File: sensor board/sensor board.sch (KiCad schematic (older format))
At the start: 25 parts, among them IC1 AD5933YRSZ, IC2 MAX86141ENP+, J1 502078-1710

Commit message: sensor board part numbers review
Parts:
- C1, C6: Digikey Part Number (none) -> 311-1729-2-ND; Field4 https://www.mouser.ee/ProductDetail/Yageo/CC0402MRX5R5BB106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 -> (none); Mouser Price/Stock (none) -> https://www.mouser.ee/ProductDetail/Yageo/CC0402MRX5R5BB106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; Price 0.23 -> 0.22
- C2: renamed from C3; Digikey Part Number (none) -> 311-1640-2-ND; Field4 https://www.mouser.ee/ProductDetail/Yageo/CC0402FRNPO9BN100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 -> (none); Mouser Price/Stock (none) -> https://www.mouser.ee/ProductDetail/Yageo/CC0402FRNPO9BN100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
- C3: renamed from C2; Digikey Part Number (none) -> 311-1438-2-ND; Field4 https://www.mouser.ee/ProductDetail/Yageo/CC0402KRX5R5BB105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 -> (none); Mouser Price/Stock (none) -> https://www.mouser.ee/ProductDetail/Yageo/CC0402KRX5R5BB105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
- C4: Digikey Part Number (none) -> 311-3479-2-ND; Field4 https://www.mouser.ee/ProductDetail/Yageo/CC0402MRX5R5BB226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 -> (none); Mouser Price/Stock (none) -> https://www.mouser.ee/ProductDetail/Yageo/CC0402MRX5R5BB226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
- C5: Digikey Part Number (none) -> 311-3340-2-ND; Field4 https://www.mouser.ee/ProductDetail/Yageo/CC0402KRX5R5BB104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 -> (none); Mouser Price/Stock (none) -> https://www.mouser.ee/ProductDetail/Yageo/CC0402KRX5R5BB104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
- D1: Field4 https://www.mouser.ee/ProductDetail/OSRAM-Opto-Semiconducto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 -> (none); Mouser Price/Stock (none) -> https://www.mouser.ee/ProductDetail/OSRAM-Opto-Semiconducto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
- D2, D3: Digikey Part Number (none) -> VEMD8080TR-ND
- IC1: Digikey Part Number (none) -> AD5933YRSZ-ND
- IC2: Digikey Part Number (none) -> MAX86141ENP+-ND
- J1: Digikey Part Number (none) -> WM14446TR-ND
- L1: footprint LQW15DN100M00D -> Horace:LQW15DN150M00D; Digikey Part Number (none) -> 490-18069-2-ND
- R1, R10, R2, R5: Digikey Part Number (none) -> 541-4062-2-ND; Field4 https://www.mouser.ee/ProductDetail/Vishay-Dale/CRCW0402000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 -> (none); Mouser Price/Stock (none) -> https://www.mouser.ee/ProductDetail/Vishay-Dale/CRCW0402000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
- R3, R4: Digikey Part Number (none) -> 541-4276-2-ND; Field4 https://www.mouser.ee/ProductDetail/Vishay-Dale/CRCW010010K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 -> (none); Mouser Price/Stock (none) -> https://www.mouser.ee/ProductDetail/Vishay-Dale/CRCW010010K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
- R6, R8, R9: Digikey Part Number (none) -> 541-4279-2-ND; Field4 https://www.mouser.ee/ProductDetail/Vishay-Dale/CRCW01001K0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 -> (none); Mouser Price/Stock (none) -> https://www.mouser.ee/ProductDetail/Vishay-Dale/CRCW01001K0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; Price 0.15 -> 0.14
- R7: Digikey Part Number (none) -> 541-4279-2-ND; Mouser Price/Stock (none) -> https://www.mouser.ee/ProductDetail/Vishay-Dale/CRCW01001K0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; Price 0.15 -> 0.14
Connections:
- net at IC1.6 (VOUT): now also L1.1
- net at L1.2: now also C2.2, TP1.1
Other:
- moved on the sheet: L1

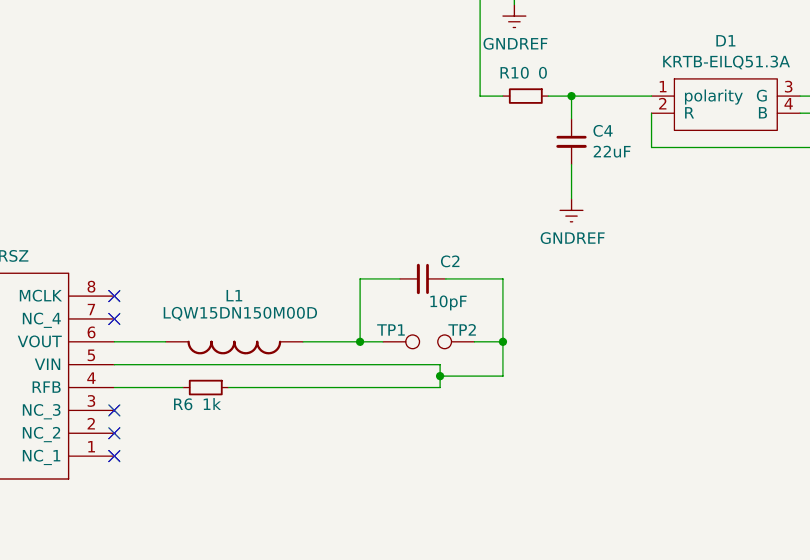
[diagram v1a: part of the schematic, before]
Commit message: added impedance probe pins
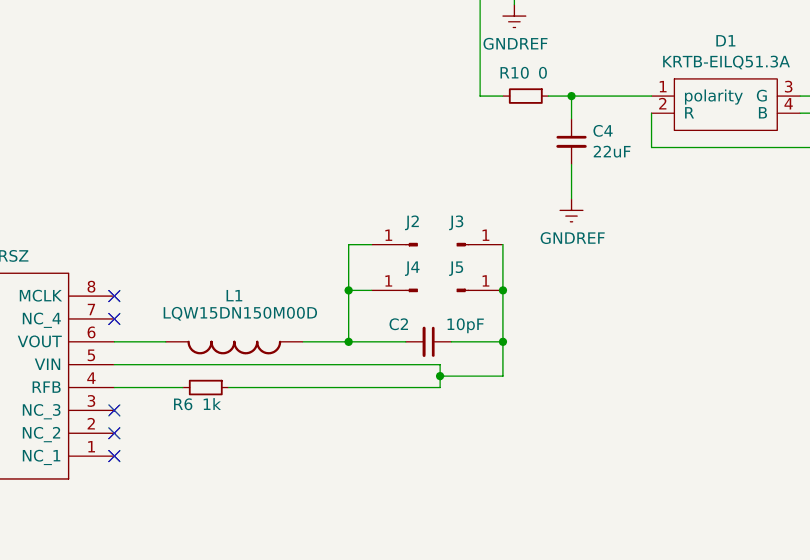
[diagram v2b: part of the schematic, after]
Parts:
- removed TP1, TP2: TestPoint, TestPoint:TestPoint_Pad_D1.5mm, symbol Connector:TestPoint
- added J2, J3, J4, J5: Probe_01_male, Horace:Probe_01_male, symbol Horace:Probe_01_male
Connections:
- net at C2.1, IC1.5 (VIN), R6.1: now also J3.1 (Pin_1), J5.1 (Pin_1)
- net at C2.2, L1.2: now also J2.1 (Pin_1), J4.1 (Pin_1)
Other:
- moved on the sheet: C2
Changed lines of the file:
@@
 L Device:C_Small C2
 U 1 1 6002A88D
-P 4250 5550
-F 0 "C2" V 4175 5625 50  0000 L CNN
-F 1 "10pF" V 4350 5575 50  0000 L CNN
-F 2 "Capacitor_SMD:C_0402_1005Metric" H 4250 5550 50  0001 C CNN
-F 3 "https://www.mouser.ee/datasheet/2/447/yageo_yago_s_a0009251638_1-1991554.pdf" H 4250 5550 50  0001 C CNN
-F 4 "https://www.mouser.ee/ProductDetail/Yageo/CC0402FRNPO9BN100/?qs=5q%252BqlK8CmJS9pmxsdlpWSg%3D%3" V 4250 5550 50  0001 C CNN "Mouser Price/Stock"
-F 5 "311-1640-2-ND" V 4250 5550 50  0001 C CNN "Digikey Part Number"
-F 6 "0.09" V 4250 5550 50  0001 C CNN "Price"
-	1    4250 5550
+P 4275 5825
+F 0 "C2" V 4200 5650 50  0000 L CNN
+F 1 "10pF" V 4200 5900 50  0000 L CNN
+F 2 "Capacitor_SMD:C_0402_1005Metric" H 4275 5825 50  0001 C CNN
+F 3 "https://www.mouser.ee/datasheet/2/447/yageo_yago_s_a0009251638_1-1991554.pdf" H 4275 5825 50  0001 C CNN
+F 4 "https://www.mouser.ee/ProductDetail/Yageo/CC0402FRNPO9BN100/?qs=5q%252BqlK8CmJS9pmxsdlpWSg%3D%3" V 4275 5825 50  0001 C CNN "Mouser Price/Stock"
+F 5 "311-1640-2-ND" V 4275 5825 50  0001 C CNN "Digikey Part Number"
+F 6 "0.09" V 4275 5825 50  0001 C CNN "Price"
+	1    4275 5825
 	0    1    1    0
 $EndComp
@@
 	4325 5975 4325 6025
 Wire Wire Line
-	4150 5550 3975 5550
-Wire Wire Line
-	3975 5550 3975 5825
-Wire Wire Line
-	3975 5825 4075 5825
-Wire Wire Line
-	4600 5550 4600 5825
-Wire Wire Line
 	4325 5975 4600 5975
 Wire Wire Line
-	4350 5550 4600 5550
-Wire Wire Line
-	4475 5825 4600 5825
-Connection ~ 4600 5825
-Wire Wire Line
-	4600 5825 4600 5975
+	4375 5825 4600 5825
 $Comp
 L Horace:MAX86141ENP+ IC2
@@
 	1    1200 1725
 	1    0    0    -1
-$EndComp
-$Comp
-L Connector:TestPoint TP1
-U 1 1 603606C3
-P 4075 5825
-F 0 "TP1" V 4025 5800 50  0000 L CNN
-F 1 "TestPoint" V 4120 6013 50  0001 L CNN
-F 2 "TestPoint:TestPoint_Pad_D1.5mm" H 4275 5825 50  0001 C CNN
-F 3 "~" H 4275 5825 50  0001 C CNN
-	1    4075 5825
-	0    1    1    0
-$EndComp
-$Comp
-L Connector:TestPoint TP2
-U 1 1 603615F7
-P 4475 5825
-F 0 "TP2" V 4525 5875 50  0000 C CNN
-F 1 "TestPoint" V 4520 6013 50  0001 L CNN
-F 2 "TestPoint:TestPoint_Pad_D1.5mm" H 4675 5825 50  0001 C CNN
-F 3 "~" H 4675 5825 50  0001 C CNN
-	1    4475 5825
-	0    -1   -1   0
 $EndComp
 $Comp
@@
 Wire Wire Line
 	2900 5825 3125 5825
-Connection ~ 3975 5825
 Wire Wire Line
 	2900 5925 4325 5925
@@
 Wire Wire Line
 	4500 4750 4600 4750
-Wire Wire Line
-	3725 5825 3975 5825
+$Comp
+L Horace:Probe_01_male J5
+U 1 1 605103DC
+P 4400 5600
+F 0 "J5" H 4400 5700 50  0000 C CNN
+F 1 "Probe_01_male" H 4508 5690 50  0001 C CNN
+F 2 "Horace:Probe_01_male" H 4400 5600 50  0001 C CNN
+F 3 "https://www.mouser.ee/datasheet/2/273/223.7-1519985.pdf" H 4400 5600 50  0001 C CNN
+F 4 "https://www.digikey.ee/products/en?keywords=3975-0-00-15-00-00-03-0" H 4400 5600 50  0001 C CNN "Mouser Price/Stock"
+F 5 "ED10387-ND" H 4400 5600 50  0001 C CNN "Digikey Part Number"
+F 6 "0.3" H 4400 5600 50  0001 C CNN "Price"
+	1    4400 5600
+	1    0    0    -1
+$EndComp
+$Comp
+L Horace:Probe_01_male J3
+U 1 1 60510E17
+P 4400 5400
+F 0 "J3" H 4400 5500 50  0000 C CNN
+F 1 "Probe_01_male" H 4508 5490 50  0001 C CNN
+F 2 "Horace:Probe_01_male" H 4400 5400 50  0001 C CNN
+F 3 "https://www.mouser.ee/datasheet/2/273/223.7-1519985.pdf" H 4400 5400 50  0001 C CNN
+F 4 "https://www.digikey.ee/products/en?keywords=3975-0-00-15-00-00-03-0" H 4400 5400 50  0001 C CNN "Mouser Price/Stock"
+F 5 "ED10387-ND" H 4400 5400 50  0001 C CNN "Digikey Part Number"
+F 6 "0.3" H 4400 5400 50  0001 C CNN "Price"
+	1    4400 5400
+	1    0    0    -1
+$EndComp
+Wire Wire Line
+	4600 5825 4600 5975
+Wire Wire Line
+	3725 5825 3925 5825
+$Comp
+L Horace:Probe_01_male J4
+U 1 1 60551210
+P 4225 5600
+F 0 "J4" H 4275 5500 50  0000 R CNN
+F 1 "Probe_01_male" H 4333 5690 50  0001 C CNN
+F 2 "Horace:Probe_01_male" H 4225 5600 50  0001 C CNN
+F 3 "https://www.mouser.ee/datasheet/2/273/223.7-1519985.pdf" H 4225 5600 50  0001 C CNN
+F 4 "https://www.digikey.ee/products/en?keywords=3975-0-00-15-00-00-03-0" H 4225 5600 50  0001 C CNN "Mouser Price/Stock"
+F 5 "ED10387-ND" H 4225 5600 50  0001 C CNN "Digikey Part Number"
+F 6 "0.3" H 4225 5600 50  0001 C CNN "Price"
+	1    4225 5600
+	-1   0    0    1
+$EndComp
+Wire Wire Line
+	4025 5400 3925 5400
+Wire Wire Line
+	3925 5400 3925 5600
+Connection ~ 3925 5825
+Wire Wire Line
+	3925 5825 4175 5825
+Wire Wire Line
+	4025 5600 3925 5600
+Connection ~ 3925 5600
+Wire Wire Line
+	3925 5600 3925 5825
+Wire Wire Line
+	4600 5400 4600 5600
+Connection ~ 4600 5825
+Connection ~ 4600 5600
+Wire Wire Line
+	4600 5600 4600 5825
 Wire Bus Line
 	2900 1425 2900 2025
 Wire Bus Line
+	1275 2125 1275 6225
+Wire Bus Line
 	4275 1425 4275 3450
-Wire Bus Line
-	1275 2125 1275 6225
+$Comp
+L Horace:Probe_01_male J2
+U 1 1 60550E5D
+P 4225 5400
+F 0 "J2" H 4275 5300 50  0000 R CNN
+F 1 "Probe_01_male" H 4333 5490 50  0001 C CNN
+F 2 "Horace:Probe_01_male" H 4225 5400 50  0001 C CNN
+F 3 "https://www.mouser.ee/datasheet/2/273/223.7-1519985.pdf" H 4225 5400 50  0001 C CNN
+F 4 "https://www.digikey.ee/products/en?keywords=3975-0-00-15-00-00-03-0" H 4225 5400 50  0001 C CNN "Mouser Price/Stock"
+F 5 "ED10387-ND" H 4225 5400 50  0001 C CNN "Digikey Part Number"
+F 6 "0.3" H 4225 5400 50  0001 C CNN "Price"
+	1    4225 5400
+	-1   0    0    1
+$EndComp
 $EndSCHEMATC

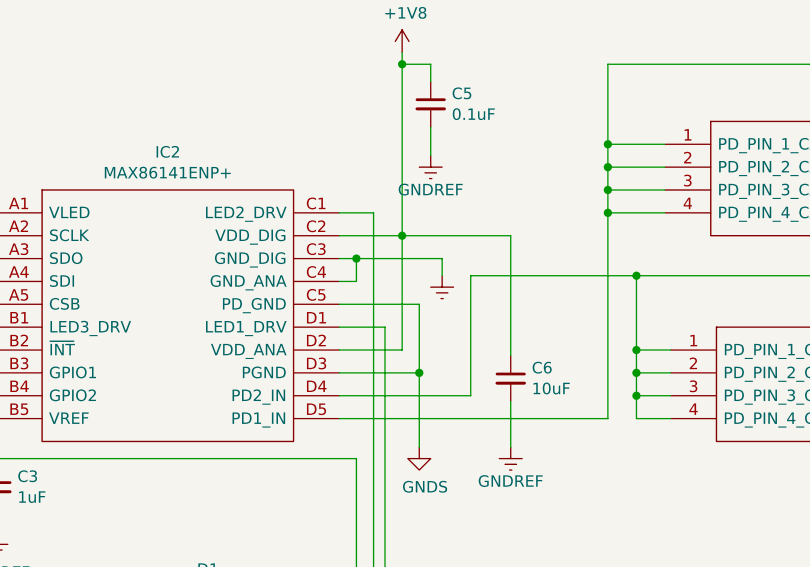
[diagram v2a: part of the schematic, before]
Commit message: added buried vias
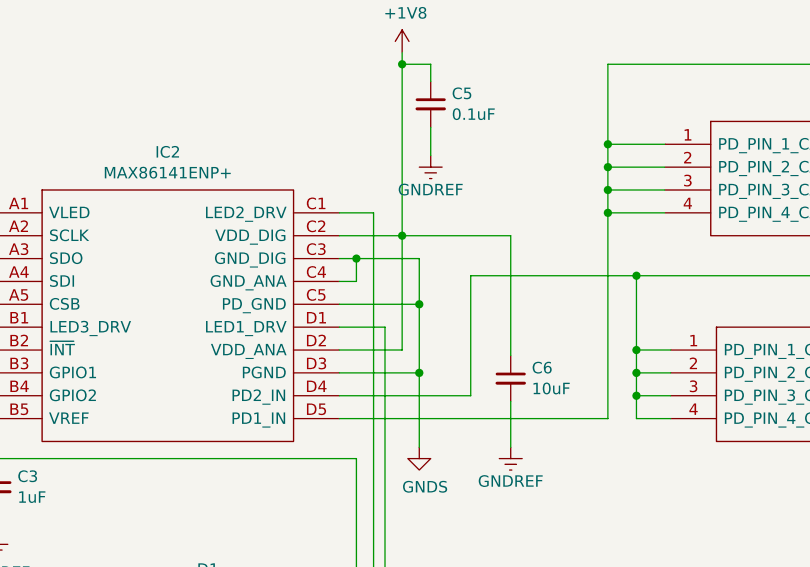
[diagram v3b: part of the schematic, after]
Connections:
- net GNDREF: no longer IC2.C3 (GND_DIG), IC2.C4 (GND_ANA)
- net GNDS: now also IC2.C3 (GND_DIG), IC2.C4 (GND_ANA)
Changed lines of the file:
@@
 	6150 3350 6500 3350
-Wire Wire Line
-	6500 3350 6500 3650
 Wire Wire Line
 	6150 3550 6425 3550
@@
 Wire Wire Line
 	6900 3775 6900 3975
-$Comp
-L power:GNDREF #PWR0115
-U 1 1 6026178A
-P 6600 3225
-F 0 "#PWR0115" H 6600 2975 50  0001 C CNN
-F 1 "GNDREF" H 6600 3075 50  0001 C CNN
-F 2 "" H 6600 3225 50  0001 C CNN
-F 3 "" H 6600 3225 50  0001 C CNN
-	1    6600 3225
-	1    0    0    -1
-$EndComp
-Wire Wire Line
-	6150 3150 6225 3150
 Wire Wire Line
 	6150 3250 6225 3250
 Wire Wire Line
 	6225 3250 6225 3150
-Connection ~ 6225 3150
 Wire Wire Line
 	6150 3850 7325 3850
@@
 Wire Wire Line
 	3400 6025 4325 6025
-Wire Wire Line
-	6600 3150 6600 3225
-Wire Wire Line
-	6225 3150 6600 3150
 $Comp
 L Horace:KRTB-EILQ51.3A D1
@@
 Wire Wire Line
 	4600 5600 4600 5825
-Wire Bus Line
-	2900 1425 2900 2025
-Wire Bus Line
-	1275 2125 1275 6225
-Wire Bus Line
-	4275 1425 4275 3450
 $Comp
 L Horace:Probe_01_male J2
@@
 	-1   0    0    1
 $EndComp
+Wire Wire Line
+	6500 3150 6500 3350
+Wire Wire Line
+	6150 3150 6225 3150
+Wire Bus Line
+	2900 1425 2900 2025
+Wire Bus Line
+	4275 1425 4275 3450
+Wire Bus Line
+	1275 2125 1275 6225
+Connection ~ 6500 3350
+Wire Wire Line
+	6500 3350 6500 3650
+Connection ~ 6225 3150
+Wire Wire Line
+	6225 3150 6500 3150
 $EndSCHEMATC
